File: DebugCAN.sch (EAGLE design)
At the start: 56 parts, among them J1 8P8C-LED, J2 MICRO-USB-RECEPTACLE47589-0001, J3 MA04-1, J5 8P8C-LED, J6 8P8C-LED, J7 8P8C-LED, U1 STM32F302C, U2 NCV7351D1E, U3 SI8621AB-B-IS, U4 AP2127N-3.3TRG1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

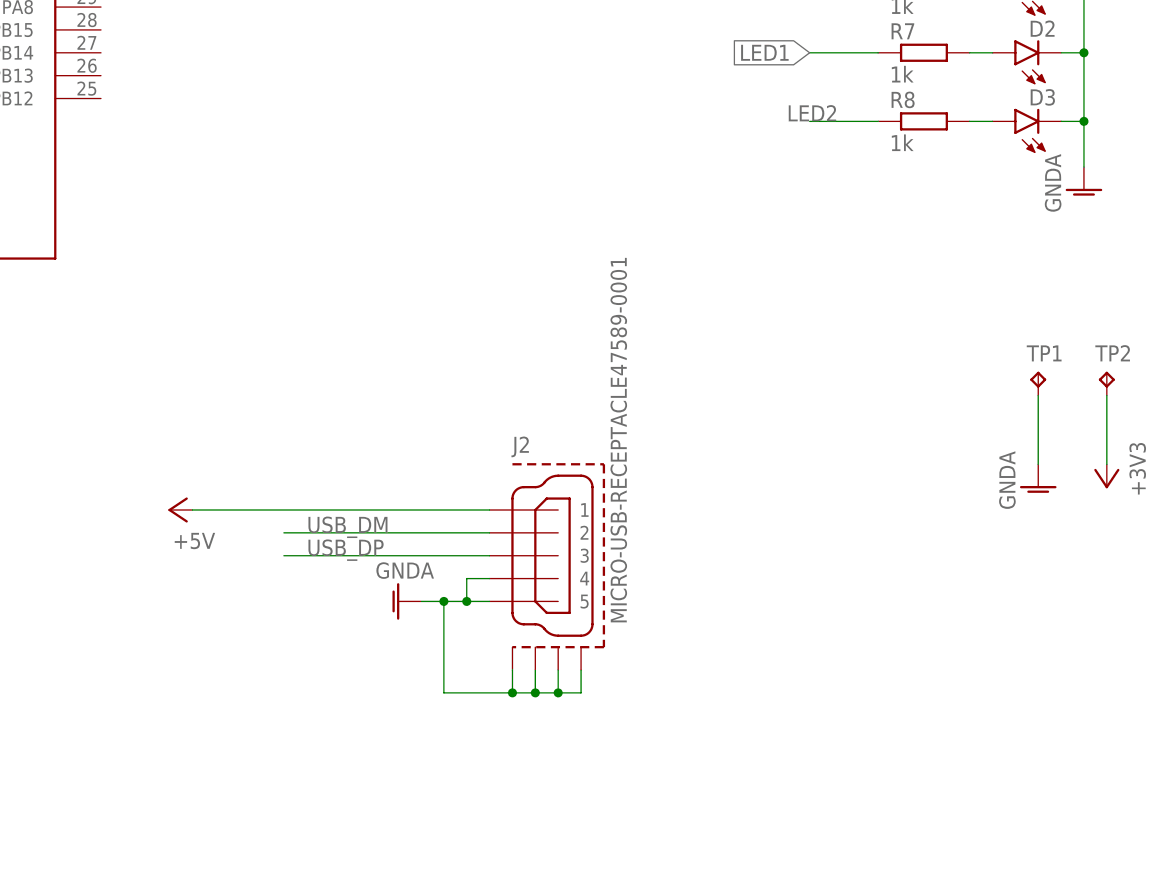
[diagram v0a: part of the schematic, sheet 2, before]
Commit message: USBの変更
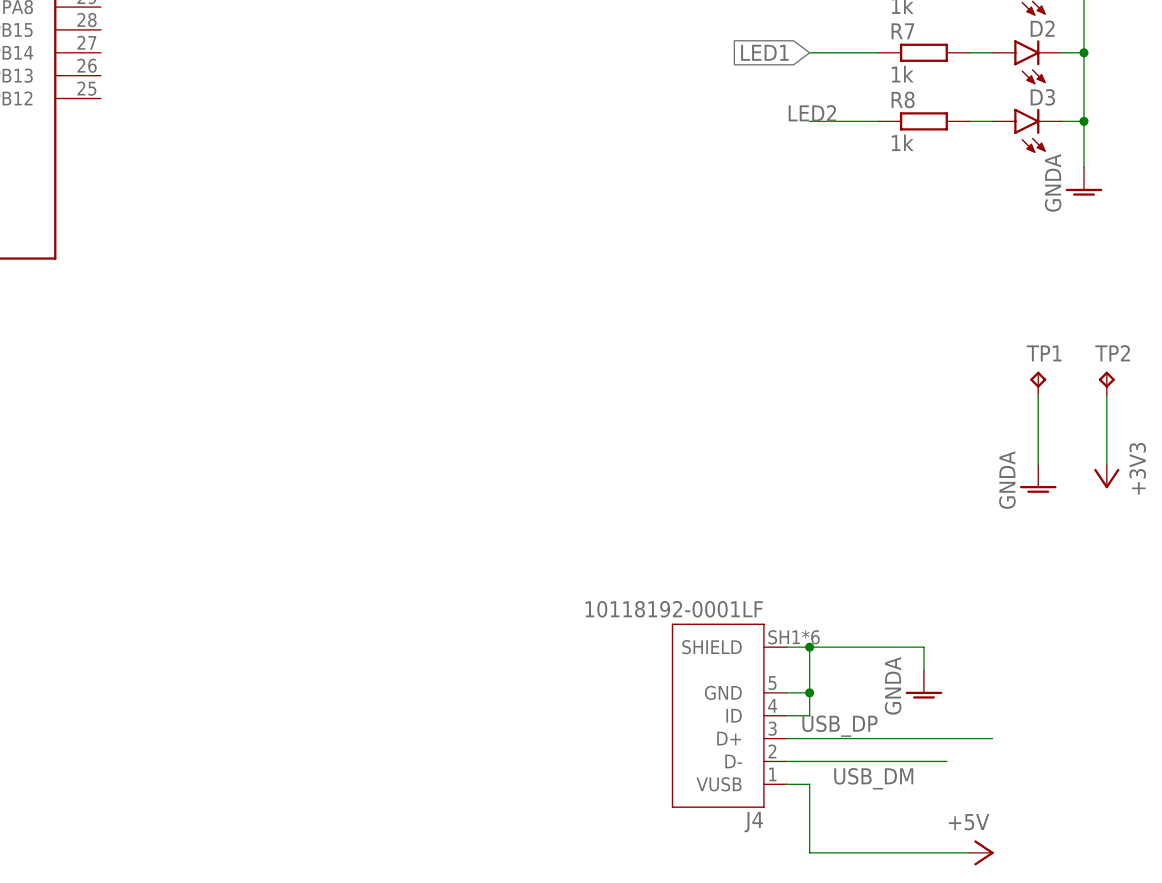
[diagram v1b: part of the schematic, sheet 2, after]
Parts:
- removed J2: MICRO-USB-RECEPTACLE47589-0001, con-molex-usb:MICRO-USB-RECEPTACLE47589-0001
- added J4: 10118192-0001LF, con-usb:10118192-0001LF
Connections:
- net +5V: now also J4.VUSB; no longer J2.1
- net GNDA: now also J4.GND, J4.ID, J4.SHIELD; no longer J2.4, J2.5, J2.GND1, J2.GND2, J2.GND3, J2.GND4
- net USB_DM: now also J4.D-; no longer J2.2
- net USB_DP: now also J4.D+; no longer J2.3
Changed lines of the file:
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@@
 <part name="GND28" library="supply1" library_urn="urn:adsk.eagle:library:371" deviceset="GNDA" device=""/>
 <part name="P+2" library="supply1" library_urn="urn:adsk.eagle:library:371" deviceset="+5V" device=""/>
-<part name="P+3" library="supply1" library_urn="urn:adsk.eagle:library:371" deviceset="+5V" device=""/>
 <part name="C7" library="rcl" deviceset="C-EU" device="C0805" value="4u7"/>
 <part name="P+5" library="supply1" library_urn="urn:adsk.eagle:library:371" deviceset="+3V3" device=""/>
@@
 <part name="P+22" library="supply1" library_urn="urn:adsk.eagle:library:371" deviceset="+3V3" device=""/>
 <part name="P+29" library="supply1" library_urn="urn:adsk.eagle:library:371" deviceset="+5V" device=""/>
-<part name="J2" library="con-molex-usb" deviceset="MICRO-USB-RECEPTACLE" device="47589-0001"/>
 <part name="C5" library="rcl" deviceset="C-EU" device="C0603" value="1u"/>
 <part name="C12" library="rcl" deviceset="C-EU" device="C0603" value="100n"/>
 <part name="J3" library="con-headers" deviceset="MA04-1" device=""/>
-<part name="GND7" library="supply1" library_urn="urn:adsk.eagle:library:371" deviceset="GNDA" device=""/>
 <part name="GND14" library="supply1" library_urn="urn:adsk.eagle:library:371" deviceset="GNDA" device=""/>
 <part name="GND15" library="supply1" library_urn="urn:adsk.eagle:library:371" deviceset="GNDA" device=""/>
@@
 <part name="H3" library="holes" library_urn="urn:adsk.eagle:library:237" deviceset="MOUNT-HOLE" device="3.2" package3d_urn="urn:adsk.eagle:package:14275/1"/>
 <part name="H4" library="holes" library_urn="urn:adsk.eagle:library:237" deviceset="MOUNT-HOLE" device="3.2" package3d_urn="urn:adsk.eagle:package:14275/1"/>
+<part name="GND32" library="supply1" library_urn="urn:adsk.eagle:library:371" deviceset="GNDA" device=""/>
+<part name="J4" library="con-usb" deviceset="10118192-0001LF" device=""/>
+<part name="P+14" library="supply1" library_urn="urn:adsk.eagle:library:371" deviceset="+5V" device=""/>
 </parts>
 <sheets>
@@
 <attribute name="VALUE" x="218.44" y="129.54" size="1.778" layer="96" rot="R90"/>
 </instance>
-<instance part="P+3" gate="1" x="154.94" y="27.94" smashed="yes" rot="R90">
-<attribute name="VALUE" x="160.02" y="25.4" size="1.778" layer="96" rot="R180"/>
-</instance>
 <instance part="C7" gate="G$1" x="274.32" y="116.84" smashed="yes">
 <attribute name="NAME" x="275.844" y="117.221" size="1.778" layer="95"/>
@@
 <attribute name="VALUE" x="60.96" y="180.34" size="1.778" layer="96" rot="R90"/>
 </instance>
-<instance part="J2" gate="G$1" x="195.58" y="22.86" smashed="yes">
-<attribute name="NAME" x="193.04" y="34.29" size="1.778" layer="95" font="vector"/>
-<attribute name="VALUE" x="205.74" y="15.24" size="1.778" layer="96" font="vector" rot="R90"/>
-</instance>
 <instance part="C5" gate="G$1" x="226.06" y="116.84" smashed="yes">
 <attribute name="NAME" x="227.584" y="117.221" size="1.778" layer="95"/>
@@
 <attribute name="NAME" x="29.21" y="183.642" size="1.778" layer="95"/>
 </instance>
-<instance part="GND7" gate="1" x="180.34" y="17.78" smashed="yes" rot="R270">
-<attribute name="VALUE" x="177.8" y="20.32" size="1.778" layer="96"/>
-</instance>
 <instance part="GND14" gate="1" x="121.92" y="48.26" smashed="yes">
 <attribute name="VALUE" x="119.38" y="45.72" size="1.778" layer="96" rot="R90"/>
@@
 <attribute name="NAME" x="285.75" y="52.07" size="1.778" layer="95" rot="R90"/>
 <attribute name="TP_SIGNAL_NAME" x="288.29" y="54.61" size="1.778" layer="97" rot="R90"/>
+</instance>
+<instance part="GND32" gate="1" x="238.76" y="7.62" smashed="yes">
+<attribute name="VALUE" x="236.22" y="5.08" size="1.778" layer="96" rot="R90"/>
+</instance>
+<instance part="J4" gate="G$1" x="215.9" y="5.08" smashed="yes" rot="R180">
+<attribute name="NAME" x="220.98618125" y="-5.601" size="1.780159375" layer="95" rot="R180"/>
+<attribute name="VALUE" x="220.988209375" y="17.8005" size="1.78086875" layer="96" rot="R180"/>
+</instance>
+<instance part="P+14" gate="1" x="246.38" y="-10.16" smashed="yes" rot="R270">
+<attribute name="VALUE" x="241.3" y="-7.62" size="1.778" layer="96"/>
 </instance>
 </instances>
@@
 </segment>
 <segment>
-<wire x1="167.64" y1="25.4" x2="190.5" y2="25.4" width="0.1524" layer="91"/>
-<pinref part="J2" gate="G$1" pin="2"/>
-<label x="170.18" y="25.4" size="1.778" layer="95"/>
-</segment>
-<segment>
 <pinref part="TP4" gate="G$1" pin="TP"/>
 <wire x1="289.56" y1="58.42" x2="302.26" y2="58.42" width="0.1524" layer="91"/>
 <label x="297.18" y="58.42" size="1.778" layer="95"/>
+</segment>
+<segment>
+<label x="228.6" y="-2.54" size="1.778" layer="95"/>
+<wire x1="223.52" y1="0" x2="241.3" y2="0" width="0.1524" layer="91"/>
+<pinref part="J4" gate="G$1" pin="D-"/>
 </segment>
 </net>
@@
 </segment>
 <segment>
-<wire x1="167.64" y1="22.86" x2="190.5" y2="22.86" width="0.1524" layer="91"/>
-<pinref part="J2" gate="G$1" pin="3"/>
-<label x="170.18" y="22.86" size="1.778" layer="95"/>
-</segment>
-<segment>
 <pinref part="TP5" gate="G$1" pin="TP"/>
 <wire x1="289.56" y1="53.34" x2="302.26" y2="53.34" width="0.1524" layer="91"/>
 <label x="297.18" y="53.34" size="1.778" layer="95"/>
+</segment>
+<segment>
+<wire x1="246.38" y1="2.54" x2="223.52" y2="2.54" width="0.1524" layer="91"/>
+<pinref part="J4" gate="G$1" pin="D+"/>
+<label x="233.68" y="5.08" size="1.778" layer="95" rot="R180"/>
 </segment>
 </net>
@@
 </segment>
 <segment>
-<wire x1="182.88" y1="17.78" x2="185.42" y2="17.78" width="0.1524" layer="91"/>
-<pinref part="J2" gate="G$1" pin="5"/>
-<pinref part="J2" gate="G$1" pin="GND4"/>
-<wire x1="185.42" y1="17.78" x2="187.96" y2="17.78" width="0.1524" layer="91"/>
-<wire x1="187.96" y1="17.78" x2="190.5" y2="17.78" width="0.1524" layer="91"/>
-<wire x1="200.66" y1="10.16" x2="200.66" y2="7.62" width="0.1524" layer="91"/>
-<wire x1="200.66" y1="7.62" x2="198.12" y2="7.62" width="0.1524" layer="91"/>
-<wire x1="198.12" y1="7.62" x2="195.58" y2="7.62" width="0.1524" layer="91"/>
-<wire x1="195.58" y1="7.62" x2="193.04" y2="7.62" width="0.1524" layer="91"/>
-<wire x1="193.04" y1="7.62" x2="185.42" y2="7.62" width="0.1524" layer="91"/>
-<wire x1="185.42" y1="7.62" x2="185.42" y2="17.78" width="0.1524" layer="91"/>
-<junction x="185.42" y="17.78"/>
-<pinref part="J2" gate="G$1" pin="GND3"/>
-<wire x1="198.12" y1="10.16" x2="198.12" y2="7.62" width="0.1524" layer="91"/>
-<junction x="198.12" y="7.62"/>
-<pinref part="J2" gate="G$1" pin="GND2"/>
-<wire x1="195.58" y1="10.16" x2="195.58" y2="7.62" width="0.1524" layer="91"/>
-<junction x="195.58" y="7.62"/>
-<pinref part="J2" gate="G$1" pin="GND1"/>
-<wire x1="193.04" y1="10.16" x2="193.04" y2="7.62" width="0.1524" layer="91"/>
-<junction x="193.04" y="7.62"/>
-<pinref part="J2" gate="G$1" pin="4"/>
-<wire x1="190.5" y1="20.32" x2="187.96" y2="20.32" width="0.1524" layer="91"/>
-<wire x1="187.96" y1="20.32" x2="187.96" y2="17.78" width="0.1524" layer="91"/>
-<junction x="187.96" y="17.78"/>
-<pinref part="GND7" gate="1" pin="GNDA"/>
-</segment>
-<segment>
 <pinref part="U1" gate="G$1" pin="VSS$1"/>
 <pinref part="GND14" gate="1" pin="GNDA"/>
@@
 <wire x1="251.46" y1="33.02" x2="251.46" y2="40.64" width="0.1524" layer="91"/>
 </segment>
+<segment>
+<pinref part="GND32" gate="1" pin="GNDA"/>
+<wire x1="226.06" y1="12.7" x2="238.76" y2="12.7" width="0.1524" layer="91"/>
+<wire x1="238.76" y1="12.7" x2="238.76" y2="10.16" width="0.1524" layer="91"/>
+<wire x1="223.52" y1="7.62" x2="226.06" y2="7.62" width="0.1524" layer="91"/>
+<wire x1="226.06" y1="7.62" x2="226.06" y2="12.7" width="0.1524" layer="91"/>
+<pinref part="J4" gate="G$1" pin="GND"/>
+<pinref part="J4" gate="G$1" pin="SHIELD"/>
+<wire x1="223.52" y1="12.7" x2="226.06" y2="12.7" width="0.1524" layer="91"/>
+<junction x="226.06" y="12.7"/>
+<pinref part="J4" gate="G$1" pin="ID"/>
+<wire x1="223.52" y1="5.08" x2="226.06" y2="5.08" width="0.1524" layer="91"/>
+<wire x1="226.06" y1="5.08" x2="226.06" y2="7.62" width="0.1524" layer="91"/>
+<junction x="226.06" y="7.62"/>
+</segment>
 </net>
 <net name="+5V" class="1">
@@
 </segment>
 <segment>
-<pinref part="P+3" gate="1" pin="+5V"/>
-<wire x1="157.48" y1="27.94" x2="190.5" y2="27.94" width="0.1524" layer="91"/>
-<pinref part="J2" gate="G$1" pin="1"/>
-</segment>
-<segment>
 <wire x1="40.64" y1="177.8" x2="63.5" y2="177.8" width="0.1524" layer="91"/>
 <pinref part="P+29" gate="1" pin="+5V"/>
@@
 <wire x1="266.7" y1="33.02" x2="266.7" y2="40.64" width="0.1524" layer="91"/>
 </segment>
-</net>
+<segment>
+<pinref part="J4" gate="G$1" pin="VUSB"/>
+<wire x1="223.52" y1="-2.54" x2="226.06" y2="-2.54" width="0.1524" layer="91"/>
+<wire x1="226.06" y1="-2.54" x2="226.06" y2="-10.16" width="0.1524" layer="91"/>
+<wire x1="226.06" y1="-10.16" x2="243.84" y2="-10.16" width="0.1524" layer="91"/>
+<pinref part="P+14" gate="1" pin="+5V"/>
+</segment>
+</net>

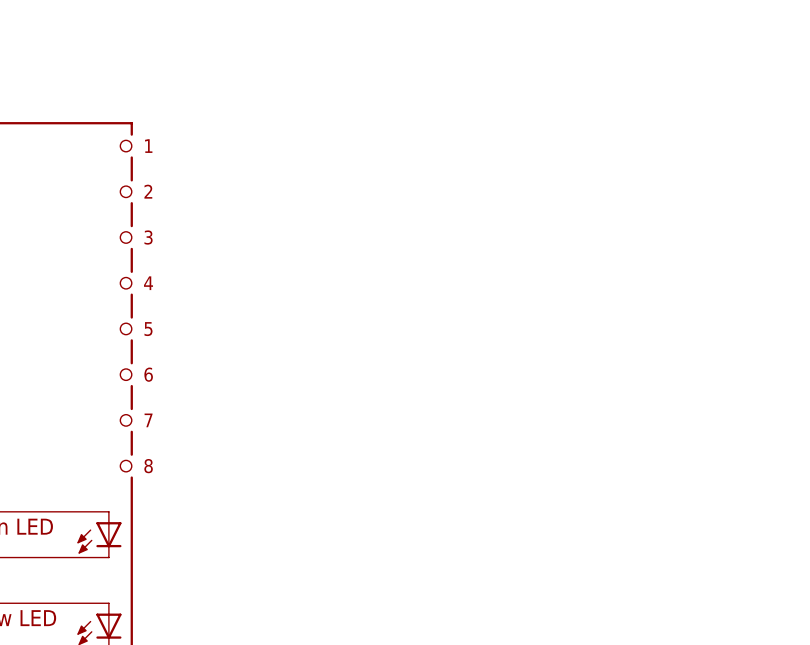
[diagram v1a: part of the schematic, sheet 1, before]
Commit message: NUC電源の管理を追加
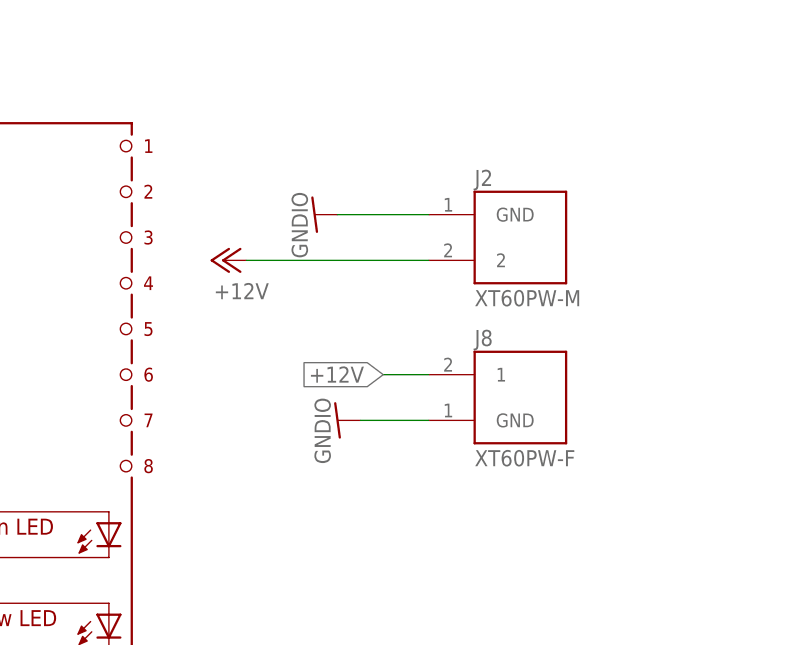
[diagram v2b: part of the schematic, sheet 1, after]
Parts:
- added J2: XT60PW-M, con-xt:XT60PW-M
- added J8: XT60PW-F, con-xt:XT60PW-F
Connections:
- net +12V: now also J2.2, J8.1
- net GNDIO: now also J2.GND, J8.GND
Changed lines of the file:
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@@
 <part name="J4" library="con-usb" deviceset="10118192-0001LF" device=""/>
 <part name="P+14" library="supply1" library_urn="urn:adsk.eagle:library:371" deviceset="+5V" device=""/>
+<part name="J2" library="con-xt" deviceset="XT60PW-M" device=""/>
+<part name="P+15" library="supply1" library_urn="urn:adsk.eagle:library:371" deviceset="+12V" device=""/>
+<part name="GND53" library="supply1" library_urn="urn:adsk.eagle:library:371" deviceset="GNDIO" device=""/>
+<part name="J8" library="con-xt" deviceset="XT60PW-F" device=""/>
+<part name="GND7" library="supply1" library_urn="urn:adsk.eagle:library:371" deviceset="GNDIO" device=""/>
 </parts>
 <sheets>
@@
 <attribute name="VALUE" x="116.332" y="15.3162" size="1.778" layer="96"/>
 </instance>
+<instance part="J2" gate="G$1" x="251.46" y="58.42" smashed="yes">
+<attribute name="NAME" x="246.37255" y="64.14338125" size="1.780609375" layer="95"/>
+<attribute name="VALUE" x="246.3718" y="50.787709375" size="1.78086875" layer="96"/>
+</instance>
+<instance part="P+15" gate="1" x="218.44" y="55.88" smashed="yes" rot="R90">
+<attribute name="VALUE" x="223.52" y="53.34" size="1.778" layer="96" rot="R180"/>
+</instance>
+<instance part="GND53" gate="G$1" x="228.6" y="60.96" smashed="yes" rot="R270">
+<attribute name="VALUE" x="226.06" y="63.5" size="1.778" layer="96" rot="R270"/>
+</instance>
+<instance part="J8" gate="G$1" x="251.46" y="40.64" smashed="yes">
+<attribute name="NAME" x="246.37255" y="46.36338125" size="1.780609375" layer="95"/>
+<attribute name="VALUE" x="246.3718" y="33.007709375" size="1.78086875" layer="96"/>
+</instance>
+<instance part="GND7" gate="G$1" x="231.14" y="38.1" smashed="yes" rot="R270">
+<attribute name="VALUE" x="228.6" y="40.64" size="1.778" layer="96" rot="R270"/>
+</instance>
 </instances>
 <busses>
@@
 <pinref part="U6" gate="G$1" pin="C"/>
 </segment>
+<segment>
+<pinref part="GND53" gate="G$1" pin="GNDIO"/>
+<pinref part="J2" gate="G$1" pin="GND"/>
+<wire x1="231.14" y1="60.96" x2="241.3" y2="60.96" width="0.1524" layer="91"/>
+</segment>
+<segment>
+<pinref part="J8" gate="G$1" pin="GND"/>
+<pinref part="GND7" gate="G$1" pin="GNDIO"/>
+<wire x1="241.3" y1="38.1" x2="233.68" y2="38.1" width="0.1524" layer="91"/>
+</segment>
 </net>
 <net name="N$3" class="0">
@@
 <pinref part="P+13" gate="1" pin="+12V"/>
 </segment>
+<segment>
+<pinref part="P+15" gate="1" pin="+12V"/>
+<pinref part="J2" gate="G$1" pin="2"/>
+<wire x1="220.98" y1="55.88" x2="241.3" y2="55.88" width="0.1524" layer="91"/>
+</segment>
+<segment>
+<pinref part="J8" gate="G$1" pin="1"/>
+<wire x1="241.3" y1="43.18" x2="236.22" y2="43.18" width="0.1524" layer="91"/>
+<label x="236.22" y="43.18" size="1.778" layer="95" rot="R180" xref="yes"/>
+</segment>
 </net>

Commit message: fainal version
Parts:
- removed J2: XT60PW-M, con-xt:XT60PW-M
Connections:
- net +12V: no longer J2.2
- net GNDIO: no longer J2.GND
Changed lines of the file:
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@@
 <part name="J4" library="con-usb" deviceset="10118192-0001LF" device=""/>
 <part name="P+14" library="supply1" library_urn="urn:adsk.eagle:library:371" deviceset="+5V" device=""/>
-<part name="J2" library="con-xt" deviceset="XT60PW-M" device=""/>
-<part name="P+15" library="supply1" library_urn="urn:adsk.eagle:library:371" deviceset="+12V" device=""/>
-<part name="GND53" library="supply1" library_urn="urn:adsk.eagle:library:371" deviceset="GNDIO" device=""/>
 <part name="J8" library="con-xt" deviceset="XT60PW-F" device=""/>
 <part name="GND7" library="supply1" library_urn="urn:adsk.eagle:library:371" deviceset="GNDIO" device=""/>
@@
 <attribute name="VALUE" x="116.332" y="15.3162" size="1.778" layer="96"/>
 </instance>
-<instance part="J2" gate="G$1" x="251.46" y="58.42" smashed="yes">
-<attribute name="NAME" x="246.37255" y="64.14338125" size="1.780609375" layer="95"/>
-<attribute name="VALUE" x="246.3718" y="50.787709375" size="1.78086875" layer="96"/>
-</instance>
-<instance part="P+15" gate="1" x="218.44" y="55.88" smashed="yes" rot="R90">
-<attribute name="VALUE" x="223.52" y="53.34" size="1.778" layer="96" rot="R180"/>
-</instance>
-<instance part="GND53" gate="G$1" x="228.6" y="60.96" smashed="yes" rot="R270">
-<attribute name="VALUE" x="226.06" y="63.5" size="1.778" layer="96" rot="R270"/>
-</instance>
 <instance part="J8" gate="G$1" x="251.46" y="40.64" smashed="yes">
 <attribute name="NAME" x="246.37255" y="46.36338125" size="1.780609375" layer="95"/>
@@
 </segment>
 <segment>
-<pinref part="GND53" gate="G$1" pin="GNDIO"/>
-<pinref part="J2" gate="G$1" pin="GND"/>
-<wire x1="231.14" y1="60.96" x2="241.3" y2="60.96" width="0.1524" layer="91"/>
-</segment>
-<segment>
 <pinref part="J8" gate="G$1" pin="GND"/>
 <pinref part="GND7" gate="G$1" pin="GNDIO"/>
@@
 </segment>
 <segment>
-<pinref part="P+15" gate="1" pin="+12V"/>
-<pinref part="J2" gate="G$1" pin="2"/>
-<wire x1="220.98" y1="55.88" x2="241.3" y2="55.88" width="0.1524" layer="91"/>
-</segment>
-<segment>
